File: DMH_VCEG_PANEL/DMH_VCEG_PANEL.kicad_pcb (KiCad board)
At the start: 2 copper layers, 150 x 200 mm, 58 parts, among them J0 Panel_GND_Solder_Wire_Pad

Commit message: Addition of manual gate ongoing
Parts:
- moved H13 15.0 mm to (85.0, 167.5)
- moved H14 15.0 mm to (70.0, 167.5)
- moved H31 15.0 mm to (115.0, 167.5)
- moved H32 15.0 mm to (130.0, 167.5)
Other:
- board text added: "4001"
- board text added: "Manual Gate"
- board text removed: "4066"

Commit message: Started placement on PCB 2
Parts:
- moved H49 0.50 mm to (150.0, 155.2)
- moved H8 0.50 mm to (50.0, 155.2)

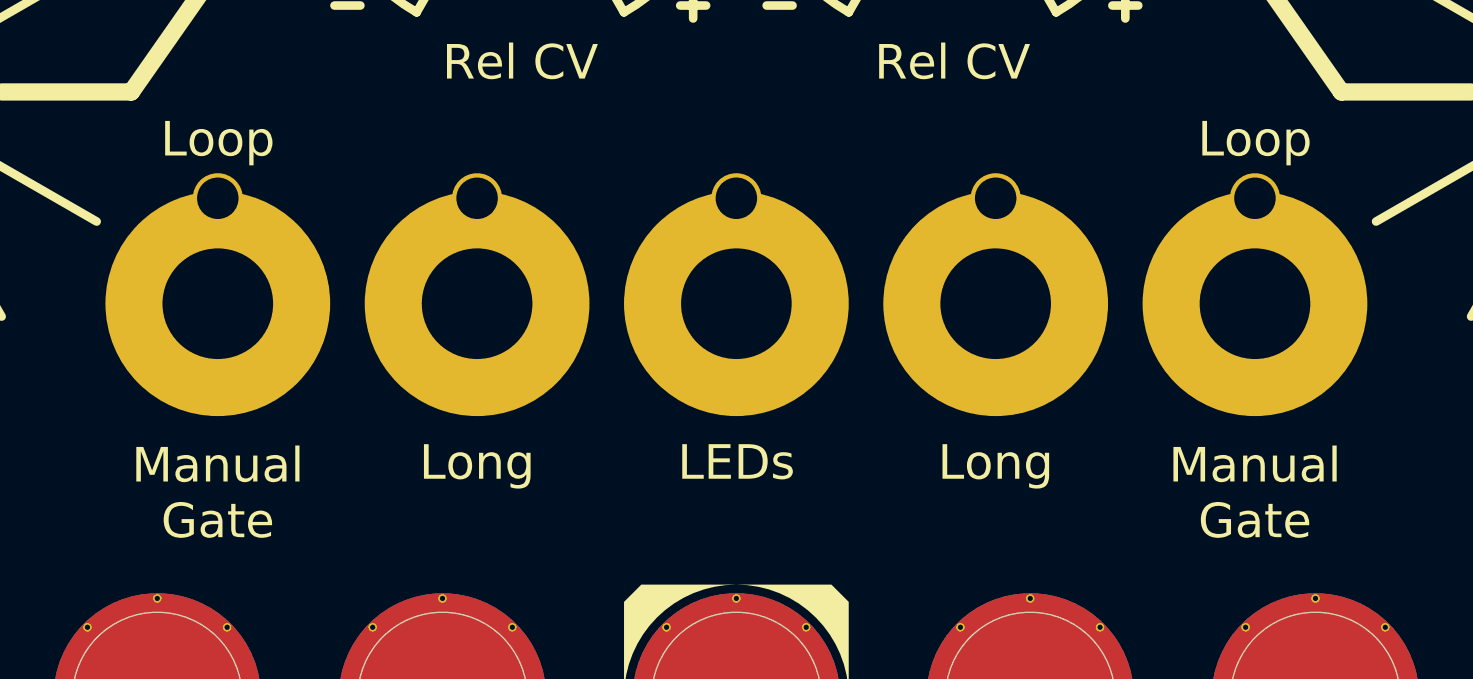
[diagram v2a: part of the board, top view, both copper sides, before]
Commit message: Added fast cap selection
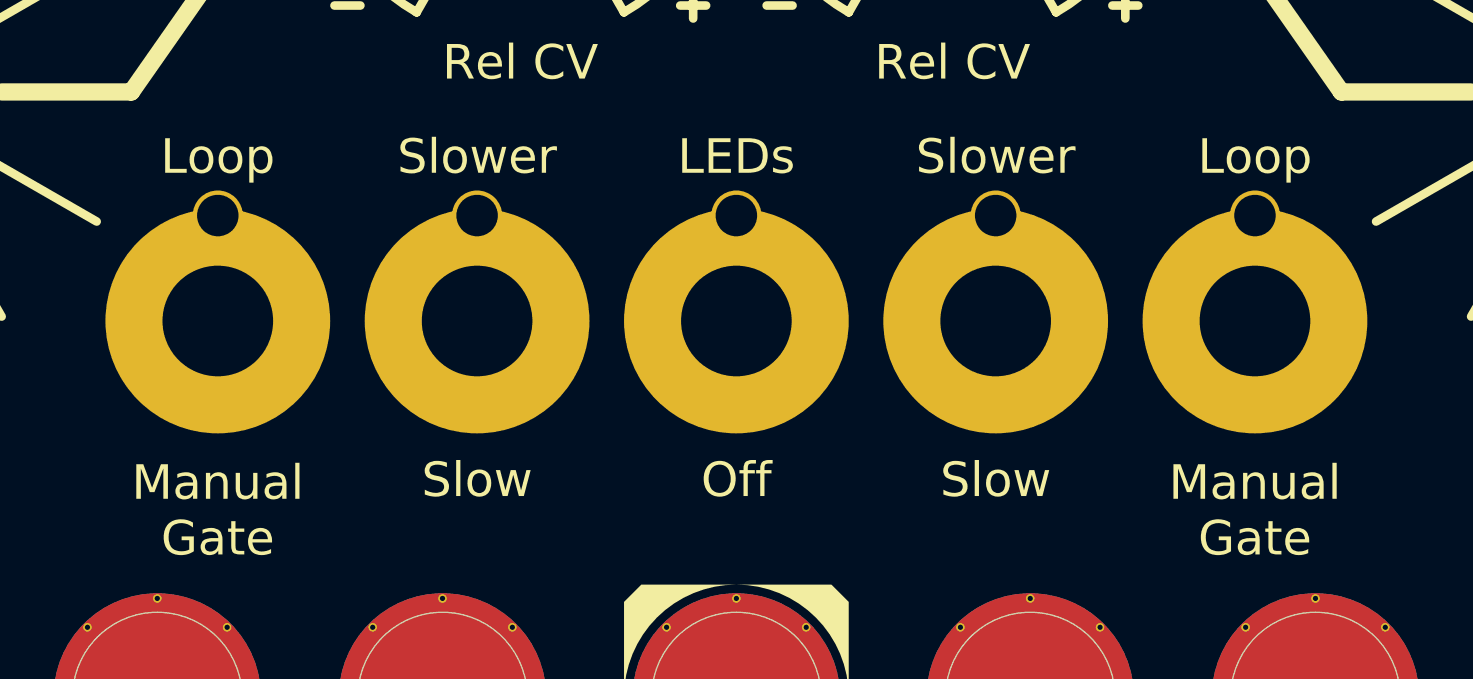
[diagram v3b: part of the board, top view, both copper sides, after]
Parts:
- H13, H31: value Long -> Slow
- moved H13 1.00 mm to (85.0, 168.5)
- moved H14 1.00 mm to (70.0, 168.5)
- moved H31 1.00 mm to (115.0, 168.5)
- moved H32 1.00 mm to (130.0, 168.5)
- moved H45 1.00 mm to (100.0, 168.5)
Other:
- board text added: "Off"
- board text added: "Slower"

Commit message: PCB 2 comp placement ongoing
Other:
- board text added: "Fast"
- board text removed: "Slower"

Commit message: Optimized PCBs
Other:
- board text added: "4066"
- board text added: "Mk1.0 - October 2025"
- board text removed: "4001"
- board text removed: "Mk1.0 - Month Year"

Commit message: Generated first gerbers
Still need to fix issues
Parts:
- H15, H29: value Att CV -> Att
- H16, H34: value Dec CV -> Dec
- H17, H37: value Sus CV -> Sus
- H18, H44: value Rel CV -> Rel

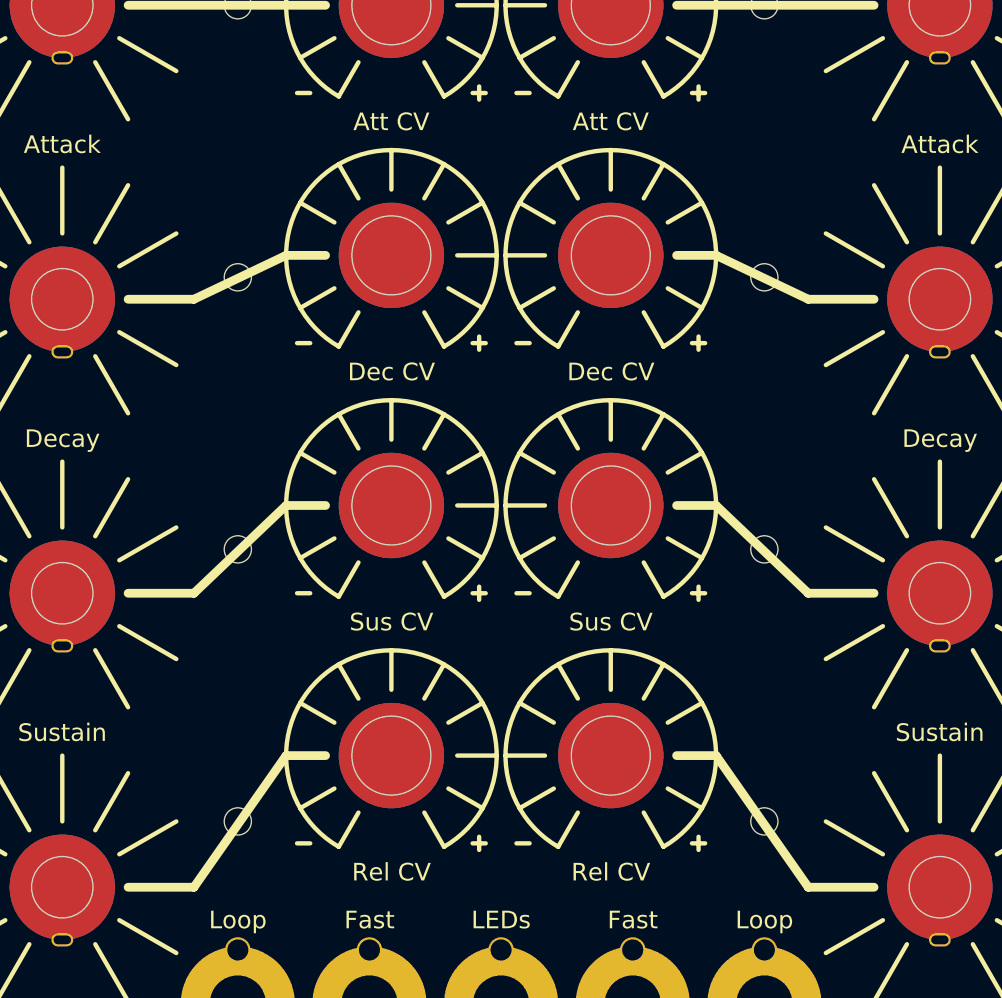
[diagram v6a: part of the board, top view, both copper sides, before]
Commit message: Reorganized repo
- Kicad 10
- Centralized and updated SynthStuff library
- Simulations folder
- Moved first version of PCB 1 to old_versions folder
- Gerbers folder
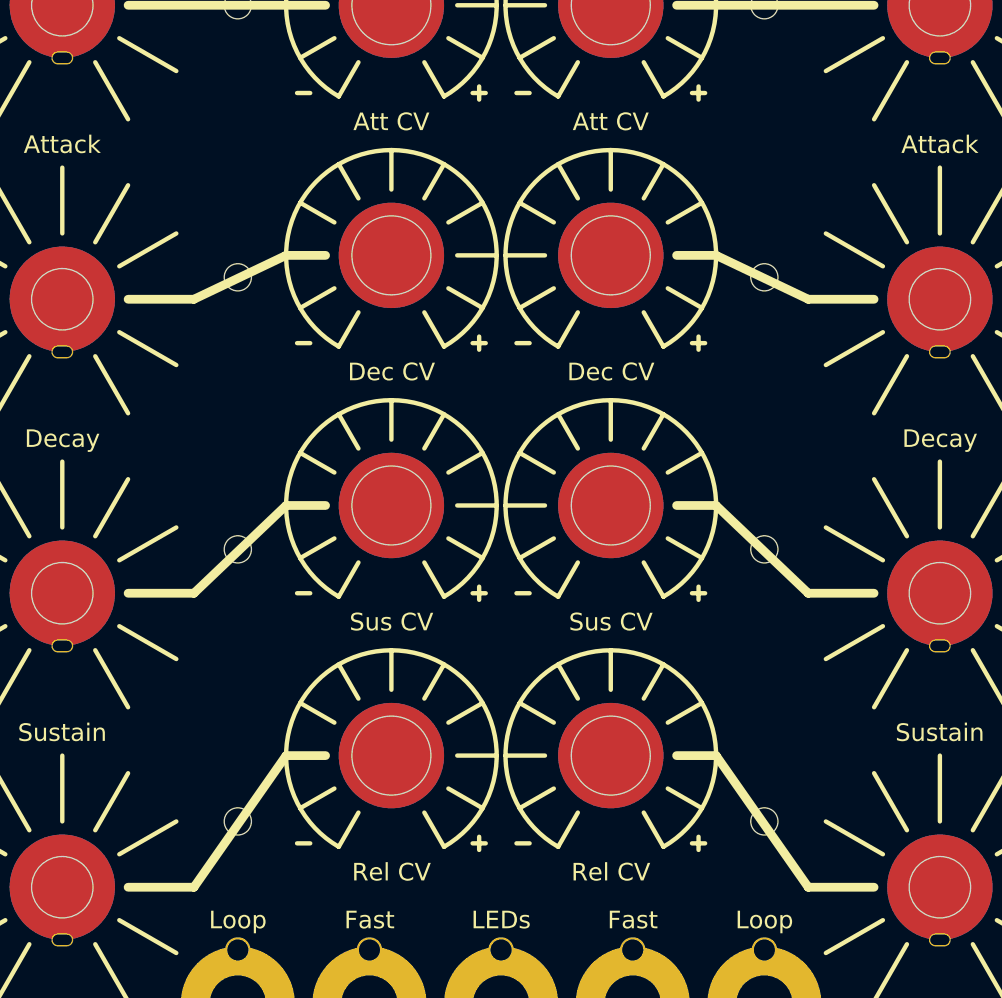
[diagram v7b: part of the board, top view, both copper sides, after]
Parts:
- H24, H25, H26, H27, H28, H33, H36, H43: footprint SynthStuff:MountingHole_LED_3mm -> SynthStuff:MountingHole_LED_3mm_R
